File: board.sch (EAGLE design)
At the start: 82 parts, among them J1 AVR_SPI_PRG_6NS, U2 USD-SOCKETNEW, U3 MAX1555, U4 TPS2112A, U6 74HC595, U7 3.3V, U8 2.8V, Y1 12.288MHz, Y2 8MHz

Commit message: Finished layout
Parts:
- added R26, R28: 10k, rcl:R-US_R0603W
- added R27: 10k, rcl:R-US_R0603
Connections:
- net CHG_B: now also U$1.PC6(OC.1A/PCINT8)
- net DS: now also U$1.PD6(RTS/AIN5/INT6)
- net ENCODER_A: now also U$1.PD1(AIN0/INT1)
- net ENCODER_B: now also U$1.PC2(PCINT11/AIN2)
- net ENCODER_S: now also U$1.PD0(OC.0B/INT0)
- net MP3_XCS: now also R26.1
- net MP3_XDCS: now also R28.1, U$1.PB7(INT4/ICP1/CLKO); no longer U$1.PC6(OC.1A/PCINT8)
- net SD_CS: now also R27.1
- net SHCP: now also U$1.PD4(INT5/AIN3)
- net STCP: now also U$1.PD5(XCK/AIN4/PCINT12)
- net VDD: now also R26.2, R27.2, R28.2
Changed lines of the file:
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@@
 <part name="R17" library="rcl" deviceset="R-US_" device="R0603W" value="100k"/>
 <part name="SUPPLY10" library="supply2" deviceset="GND" device=""/>
+<part name="R26" library="rcl" deviceset="R-US_" device="R0603W" value="10k"/>
+<part name="R27" library="rcl" deviceset="R-US_" device="R0603" value="10k"/>
+<part name="R28" library="rcl" deviceset="R-US_" device="R0603W" value="10k"/>
+<part name="SUPPLY14" library="supply2" deviceset="VDD" device=""/>
+<part name="SUPPLY19" library="supply2" deviceset="VDD" device=""/>
+<part name="SUPPLY52" library="supply2" deviceset="VDD" device=""/>
 </parts>
 <sheets>
@@
 <instance part="R17" gate="G$1" x="187.96" y="27.94" rot="R90"/>
 <instance part="SUPPLY10" gate="GND" x="180.34" y="20.32"/>
+<instance part="R26" gate="G$1" x="104.14" y="88.9"/>
+<instance part="R27" gate="G$1" x="104.14" y="83.82"/>
+<instance part="R28" gate="G$1" x="99.06" y="66.04"/>
+<instance part="SUPPLY14" gate="G$1" x="104.14" y="68.58"/>
+<instance part="SUPPLY19" gate="G$1" x="111.76" y="88.9" rot="R270"/>
+<instance part="SUPPLY52" gate="G$1" x="111.76" y="83.82" rot="R270"/>
 </instances>
 <busses>
@@
 <pinref part="U$2" gate="G$1" pin="TEST"/>
 <pinref part="SUPPLY5" gate="G$1" pin="VDD"/>
+</segment>
+<segment>
+<pinref part="R28" gate="G$1" pin="2"/>
+<pinref part="SUPPLY14" gate="G$1" pin="VDD"/>
+</segment>
+<segment>
+<pinref part="R26" gate="G$1" pin="2"/>
+<pinref part="SUPPLY19" gate="G$1" pin="VDD"/>
+</segment>
+<segment>
+<pinref part="R27" gate="G$1" pin="2"/>
+<pinref part="SUPPLY52" gate="G$1" pin="VDD"/>
 </segment>
 </net>
@@
 </segment>
 <segment>
-<wire x1="91.44" y1="66.04" x2="96.52" y2="66.04" width="0.1524" layer="91"/>
-<label x="93.98" y="66.04" size="1.778" layer="95"/>
+<label x="81.28" y="91.44" size="1.778" layer="95"/>
+<pinref part="U$1" gate="G$1" pin="PC6(OC.1A/PCINT8)"/>
+<wire x1="78.74" y1="91.44" x2="88.9" y2="91.44" width="0.1524" layer="91"/>
 </segment>
 </net>
@@
 <label x="81.28" y="88.9" size="1.778" layer="95"/>
 <pinref part="U$1" gate="G$1" pin="PC7(INT4/ICP1/CLKO)"/>
-<wire x1="78.74" y1="88.9" x2="88.9" y2="88.9" width="0.1524" layer="91"/>
+<pinref part="R26" gate="G$1" pin="1"/>
+<wire x1="99.06" y1="88.9" x2="78.74" y2="88.9" width="0.1524" layer="91"/>
 </segment>
 <segment>
@@
 <net name="MP3_XDCS" class="0">
 <segment>
-<label x="81.28" y="91.44" size="1.778" layer="95"/>
-<pinref part="U$1" gate="G$1" pin="PC6(OC.1A/PCINT8)"/>
-<wire x1="78.74" y1="91.44" x2="88.9" y2="91.44" width="0.1524" layer="91"/>
-</segment>
-<segment>
 <pinref part="U$2" gate="G$1" pin="XDCS"/>
 <wire x1="198.12" y1="58.42" x2="190.5" y2="58.42" width="0.1524" layer="91"/>
 <label x="190.5" y="58.42" size="1.778" layer="95"/>
 </segment>
+<segment>
+<pinref part="U$1" gate="G$1" pin="PB7(INT4/ICP1/CLKO)"/>
+<wire x1="78.74" y1="66.04" x2="93.98" y2="66.04" width="0.1524" layer="91"/>
+<label x="81.28" y="66.04" size="1.778" layer="95"/>
+<pinref part="R28" gate="G$1" pin="1"/>
+</segment>
 </net>
 <net name="MP3_DREQ" class="0">
@@
 </segment>
 <segment>
-<wire x1="91.44" y1="43.18" x2="96.52" y2="43.18" width="0.1524" layer="91"/>
-<label x="93.98" y="43.18" size="1.778" layer="95"/>
+<label x="83.82" y="50.8" size="1.778" layer="95"/>
+<pinref part="U$1" gate="G$1" pin="PD4(INT5/AIN3)"/>
+<wire x1="78.74" y1="50.8" x2="88.9" y2="50.8" width="0.1524" layer="91"/>
 </segment>
 </net>
@@
 </segment>
 <segment>
-<wire x1="91.44" y1="68.58" x2="96.52" y2="68.58" width="0.1524" layer="91"/>
-<label x="93.98" y="68.58" size="1.778" layer="95"/>
+<label x="83.82" y="48.26" size="1.778" layer="95"/>
+<pinref part="U$1" gate="G$1" pin="PD5(XCK/AIN4/PCINT12)"/>
+<wire x1="78.74" y1="48.26" x2="88.9" y2="48.26" width="0.1524" layer="91"/>
 </segment>
 </net>
@@
 </segment>
 <segment>
-<wire x1="91.44" y1="63.5" x2="96.52" y2="63.5" width="0.1524" layer="91"/>
-<label x="93.98" y="63.5" size="1.778" layer="95"/>
+<label x="83.82" y="45.72" size="1.778" layer="95"/>
+<pinref part="U$1" gate="G$1" pin="PD6(RTS/AIN5/INT6)"/>
+<wire x1="78.74" y1="45.72" x2="88.9" y2="45.72" width="0.1524" layer="91"/>
 </segment>
 </net>
@@
 </segment>
 <segment>
-<wire x1="78.74" y1="83.82" x2="88.9" y2="83.82" width="0.1524" layer="91"/>
 <label x="83.82" y="83.82" size="1.778" layer="95"/>
 <pinref part="U$1" gate="G$1" pin="PB0(SS/PCINT0)"/>
+<pinref part="R27" gate="G$1" pin="1"/>
+<wire x1="99.06" y1="83.82" x2="78.74" y2="83.82" width="0.1524" layer="91"/>
 </segment>
 </net>
@@
 </segment>
 <segment>
-<wire x1="109.22" y1="104.14" x2="119.38" y2="104.14" width="0.1524" layer="91"/>
-<label x="111.76" y="104.14" size="1.778" layer="95"/>
+<wire x1="78.74" y1="58.42" x2="88.9" y2="58.42" width="0.1524" layer="91"/>
+<label x="81.28" y="58.42" size="1.778" layer="95"/>
+<pinref part="U$1" gate="G$1" pin="PD1(AIN0/INT1)"/>
 </segment>
 </net>
@@
 </segment>
 <segment>
-<wire x1="109.22" y1="99.06" x2="119.38" y2="99.06" width="0.1524" layer="91"/>
-<label x="111.76" y="99.06" size="1.778" layer="95"/>
+<label x="81.28" y="99.06" size="1.778" layer="95"/>
+<pinref part="U$1" gate="G$1" pin="PC2(PCINT11/AIN2)"/>
+<wire x1="78.74" y1="99.06" x2="88.9" y2="99.06" width="0.1524" layer="91"/>
 </segment>
 </net>
@@
 </segment>
 <segment>
-<wire x1="109.22" y1="101.6" x2="119.38" y2="101.6" width="0.1524" layer="91"/>
-<label x="111.76" y="101.6" size="1.778" layer="95"/>
+<wire x1="78.74" y1="60.96" x2="88.9" y2="60.96" width="0.1524" layer="91"/>
+<label x="81.28" y="60.96" size="1.778" layer="95"/>
+<pinref part="U$1" gate="G$1" pin="PD0(OC.0B/INT0)"/>
 </segment>
 </net>
@@
 <label x="132.08" y="43.18" size="1.778" layer="95" rot="R180"/>
 </segment>
-<segment>
-<wire x1="91.44" y1="106.68" x2="101.6" y2="106.68" width="0.1524" layer="91"/>
-<label x="93.98" y="106.68" size="1.778" layer="95"/>
-</segment>
-</net>
+</net>

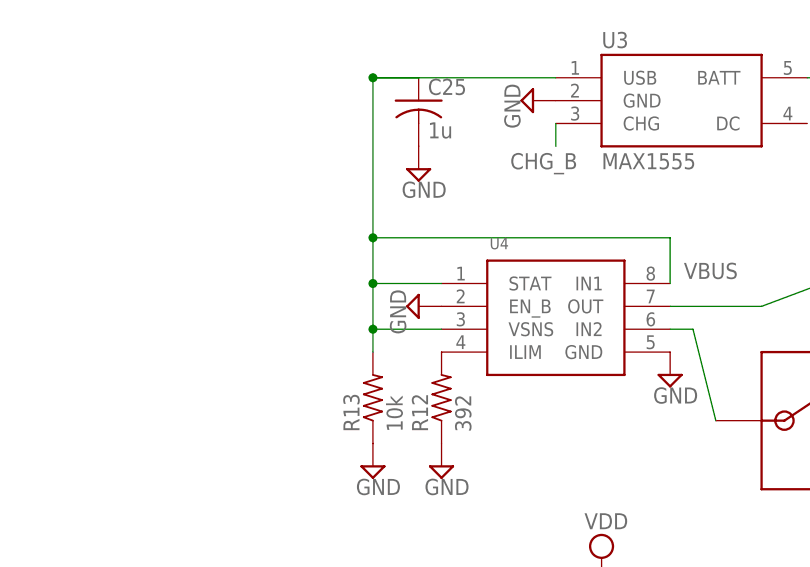
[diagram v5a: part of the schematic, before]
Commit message: Not sure why I shorted VDD with an open-drain output to ground.
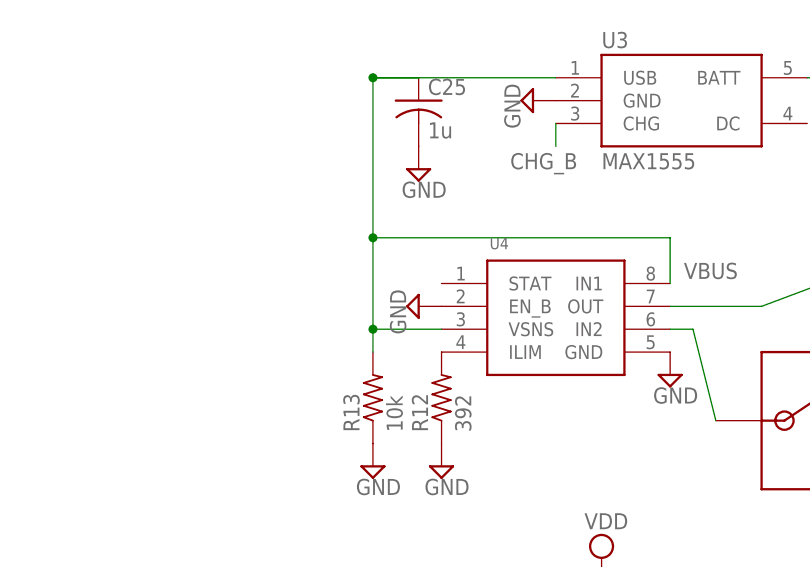
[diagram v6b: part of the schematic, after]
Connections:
- net VBUS: no longer U4.STAT
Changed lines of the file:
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@@
 <wire x1="60.96" y1="142.24" x2="53.34" y2="142.24" width="0.1524" layer="91"/>
 <wire x1="53.34" y1="142.24" x2="53.34" y2="139.7" width="0.1524" layer="91"/>
-<pinref part="U4" gate="G$1" pin="STAT"/>
-<wire x1="60.96" y1="147.32" x2="53.34" y2="147.32" width="0.1524" layer="91"/>
-<wire x1="53.34" y1="147.32" x2="53.34" y2="142.24" width="0.1524" layer="91"/>
 <junction x="53.34" y="142.24"/>
-<wire x1="53.34" y1="147.32" x2="53.34" y2="152.4" width="0.1524" layer="91"/>
-<junction x="53.34" y="147.32"/>
+<wire x1="53.34" y1="142.24" x2="53.34" y2="152.4" width="0.1524" layer="91"/>
 <pinref part="U4" gate="G$1" pin="IN1"/>
 <wire x1="53.34" y1="152.4" x2="86.36" y2="152.4" width="0.1524" layer="91"/>

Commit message: Switched to 0603W packages for audio path resistors
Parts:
- R2, R3, R5, R6, R7, R8: device rcl:R-US_R0603 -> rcl:R-US_R0603W
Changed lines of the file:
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@@
 <grid distance="0.1" unitdist="inch" unit="inch" style="lines" multiple="1" display="no" altdistance="0.01" altunitdist="inch" altunit="inch"/>
 <layers>
-<layer number="1" name="Top" color="4" fill="1" visible="no" active="no"/>
-<layer number="16" name="Bottom" color="1" fill="1" visible="no" active="no"/>
-<layer number="17" name="Pads" color="2" fill="1" visible="no" active="no"/>
-<layer number="18" name="Vias" color="2" fill="1" visible="no" active="no"/>
-<layer number="19" name="Unrouted" color="6" fill="1" visible="no" active="no"/>
-<layer number="20" name="Dimension" color="15" fill="1" visible="no" active="no"/>
-<layer number="21" name="tPlace" color="14" fill="1" visible="no" active="no"/>
-<layer number="22" name="bPlace" color="7" fill="1" visible="no" active="no"/>
-<layer number="23" name="tOrigins" color="15" fill="1" visible="no" active="no"/>
-<layer number="24" name="bOrigins" color="15" fill="1" visible="no" active="no"/>
-<layer number="25" name="tNames" color="7" fill="1" visible="no" active="no"/>
-<layer number="26" name="bNames" color="7" fill="1" visible="no" active="no"/>
-<layer number="27" name="tValues" color="7" fill="1" visible="no" active="no"/>
-<layer number="28" name="bValues" color="7" fill="1" visible="no" active="no"/>
+<layer number="1" name="Top" color="4" fill="1" visible="yes" active="no"/>
+<layer number="16" name="Bottom" color="1" fill="1" visible="yes" active="no"/>
+<layer number="17" name="Pads" color="2" fill="1" visible="yes" active="no"/>
+<layer number="18" name="Vias" color="2" fill="1" visible="yes" active="no"/>
+<layer number="19" name="Unrouted" color="6" fill="1" visible="yes" active="no"/>
+<layer number="20" name="Dimension" color="15" fill="1" visible="yes" active="no"/>
+<layer number="21" name="tPlace" color="14" fill="1" visible="yes" active="no"/>
+<layer number="22" name="bPlace" color="7" fill="1" visible="yes" active="no"/>
+<layer number="23" name="tOrigins" color="15" fill="1" visible="yes" active="no"/>
+<layer number="24" name="bOrigins" color="15" fill="1" visible="yes" active="no"/>
+<layer number="25" name="tNames" color="7" fill="1" visible="yes" active="no"/>
+<layer number="26" name="bNames" color="7" fill="1" visible="yes" active="no"/>
+<layer number="27" name="tValues" color="7" fill="1" visible="yes" active="no"/>
+<layer number="28" name="bValues" color="7" fill="1" visible="yes" active="no"/>
 <layer number="29" name="tStop" color="7" fill="3" visible="no" active="no"/>
 <layer number="30" name="bStop" color="7" fill="6" visible="no" active="no"/>
@@
 <layer number="35" name="tGlue" color="7" fill="4" visible="no" active="no"/>
 <layer number="36" name="bGlue" color="7" fill="5" visible="no" active="no"/>
-<layer number="37" name="tTest" color="7" fill="1" visible="no" active="no"/>
-<layer number="38" name="bTest" color="7" fill="1" visible="no" active="no"/>
+<layer number="37" name="tTest" color="7" fill="1" visible="yes" active="no"/>
+<layer number="38" name="bTest" color="7" fill="1" visible="yes" active="no"/>
 <layer number="39" name="tKeepout" color="4" fill="11" visible="no" active="no"/>
 <layer number="40" name="bKeepout" color="1" fill="11" visible="no" active="no"/>
@@
 <layer number="44" name="Drills" color="7" fill="1" visible="no" active="no"/>
 <layer number="45" name="Holes" color="7" fill="1" visible="no" active="no"/>
-<layer number="46" name="Milling" color="3" fill="1" visible="no" active="no"/>
-<layer number="47" name="Measures" color="7" fill="1" visible="no" active="no"/>
-<layer number="48" name="Document" color="7" fill="1" visible="no" active="no"/>
-<layer number="49" name="Reference" color="7" fill="1" visible="no" active="no"/>
-<layer number="50" name="dxf" color="7" fill="1" visible="no" active="no"/>
-<layer number="51" name="tDocu" color="7" fill="1" visible="no" active="no"/>
-<layer number="52" name="bDocu" color="7" fill="1" visible="no" active="no"/>
-<layer number="53" name="tGND_GNDA" color="7" fill="9" visible="no" active="no"/>
-<layer number="54" name="bGND_GNDA" color="1" fill="9" visible="no" active="no"/>
-<layer number="56" name="wert" color="7" fill="1" visible="no" active="no"/>
+<layer number="46" name="Milling" color="3" fill="1" visible="yes" active="no"/>
+<layer number="47" name="Measures" color="7" fill="1" visible="yes" active="no"/>
+<layer number="48" name="Document" color="7" fill="1" visible="yes" active="no"/>
+<layer number="49" name="Reference" color="7" fill="1" visible="yes" active="no"/>
+<layer number="50" name="dxf" color="7" fill="1" visible="yes" active="no"/>
+<layer number="51" name="tDocu" color="7" fill="1" visible="yes" active="no"/>
+<layer number="52" name="bDocu" color="7" fill="1" visible="yes" active="no"/>
+<layer number="53" name="tGND_GNDA" color="7" fill="9" visible="yes" active="no"/>
+<layer number="54" name="bGND_GNDA" color="1" fill="9" visible="yes" active="no"/>
+<layer number="56" name="wert" color="7" fill="1" visible="yes" active="no"/>
 <layer number="91" name="Nets" color="2" fill="1" visible="yes" active="yes"/>
 <layer number="92" name="Busses" color="1" fill="1" visible="yes" active="yes"/>
@@
 <part name="C11" library="rcl" deviceset="C-US" device="C0603K" value="0.1u"/>
 <part name="SUPPLY7" library="supply2" deviceset="GND" device=""/>
-<part name="R2" library="rcl" deviceset="R-US_" device="R0603" value="10"/>
-<part name="R3" library="rcl" deviceset="R-US_" device="R0603" value="10"/>
+<part name="R2" library="rcl" deviceset="R-US_" device="R0603W" value="10"/>
+<part name="R3" library="rcl" deviceset="R-US_" device="R0603W" value="10"/>
 <part name="R4" library="rcl" deviceset="R-US_" device="R0603W" value="10"/>
 <part name="C12" library="rcl" deviceset="C-US" device="C0603K" value="47n"/>
@@
 <part name="C14" library="rcl" deviceset="C-US" device="C0603K" value="10n"/>
 <part name="SUPPLY8" library="supply2" deviceset="GND" device=""/>
-<part name="R6" library="rcl" deviceset="R-US_" device="R0603" value="100"/>
-<part name="R5" library="rcl" deviceset="R-US_" device="R0603" value="100"/>
+<part name="R6" library="rcl" deviceset="R-US_" device="R0603W" value="100"/>
+<part name="R5" library="rcl" deviceset="R-US_" device="R0603W" value="100"/>
 <part name="C15" library="rcl" deviceset="C-US" device="C0603K" value="10u"/>
 <part name="C16" library="rcl" deviceset="C-US" device="C0603K" value="10u"/>
-<part name="R7" library="rcl" deviceset="R-US_" device="R0603" value="10k"/>
-<part name="R8" library="rcl" deviceset="R-US_" device="R0603" value="10k"/>
+<part name="R7" library="rcl" deviceset="R-US_" device="R0603W" value="10k"/>
+<part name="R8" library="rcl" deviceset="R-US_" device="R0603W" value="10k"/>
 <part name="SUPPLY11" library="supply2" deviceset="GND" device=""/>
 <part name="SUPPLY9" library="supply2" deviceset="GND" device=""/>
